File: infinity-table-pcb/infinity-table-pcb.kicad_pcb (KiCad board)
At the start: 2 copper layers, 40 x 48.9 mm, 10 parts, among them J1 PJ-063AH, J2 Conn_01x05_Male, J3 Conn_01x10_Male

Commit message: pcb first version done, but need to rework a bit
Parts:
- removed C2: 100nF, Capacitor_SMD:C_0805_2012Metric
- removed IO2, IO3, IO5, IO6: SolderJumper_3_Open, Jumper:SolderJumper-3_P1.3mm_Open_Pad1.0x1.5mm
- added C3: 0,1uF, Capacitor_SMD:C_0805_2012Metric, F.Cu at (156.5, 116.1)
- added C4: 1nF, Capacitor_SMD:C_0805_2012Metric, B.Cu at (125.8, 108.0)
- added C5: 1nF, Capacitor_SMD:C_0805_2012Metric, B.Cu at (126.2, 91.7)
- added R1: R, Resistor_SMD:R_0805_2012Metric, F.Cu at (157.5, 104.3)
- added RV1: R_Potentiometer, Connector_PinHeader_2.54mm:PinHeader_1x03_P2.54mm_Vertical, B.Cu at (113.8, 76.7)
- added SW1: SW_Push_Dual, kicad-ss-libs:Push Button 12x12mm, F.Cu at (116.6, 108.0)
- added SW2: SW_Push_Dual, kicad-ss-libs:Push Button 12x12mm, F.Cu at (116.6, 89.9)
- added U1: TXS0108EPW, Package_SO:TSSOP-20_4.4x6.5mm_P0.65mm, F.Cu at (154.6, 110.2)
- A1, J3: moved to B.Cu
- C1: value 100nF -> 0,1uF
- J1: footprint SS_connectors:CUI_PJ-063AH-1 -> kicad-ss-libs:CUI_PJ-063AH; moved to B.Cu
- J2: value Conn_01x05_Male -> Conn_01x04_Male; footprint Connector_PinHeader_2.54mm:PinHeader_1x05_P2.54mm_Vertical -> Connector_PinHeader_2.54mm:PinHeader_1x04_P2.54mm_Vertical; moved to B.Cu
- moved C1 39.0 mm to (153.5, 116.1), turned to 90 degrees
- moved J2 31.4 mm to (162.8, 87.6)
- moved J1 28.6 mm to (155.9, 77.7), turned to 0 degrees
- moved A1 16.9 mm to (146.0, 79.8), turned to 180 degrees
- moved J3 2.96 mm to (162.8, 101.1)
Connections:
- A1 pad 1: D1 -> unconnected-(A1-Pad1)
- A1 pad 10: (no net) -> Net-(A1-Pad10)
- A1 pad 11: (no net) -> Net-(A1-Pad11)
- A1 pad 12: D9 -> Net-(A1-Pad12)
- A1 pad 13: D10 -> Net-(A1-Pad13)
- A1 pad 14: (no net) -> Net-(A1-Pad14)
- A1 pad 15: (no net) -> Net-(A1-Pad15)
- A1 pad 16: (no net) -> Net-(A1-Pad16)
- A1 pad 17: (no net) -> unconnected-(A1-Pad17)
- A1 pad 18: (no net) -> unconnected-(A1-Pad18)
- A1 pad 19: (no net) -> Net-(A1-Pad19)
- A1 pad 2: D0 -> unconnected-(A1-Pad2)
- A1 pad 20: (no net) -> unconnected-(A1-Pad20)
- A1 pad 21: Net-(A1-Pad21) -> unconnected-(A1-Pad21)
- A1 pad 22: Net-(A1-Pad22) -> unconnected-(A1-Pad22)
- A1 pad 23: (no net) -> unconnected-(A1-Pad23)
- A1 pad 24: Net-(A1-Pad24) -> unconnected-(A1-Pad24)
- A1 pad 25: Net-(A1-Pad25) -> unconnected-(A1-Pad25)
- A1 pad 26: (no net) -> unconnected-(A1-Pad26)
- A1 pad 27: Net-(A1-Pad27) -> +5V
- A1 pad 28: (no net) -> unconnected-(A1-Pad28)
- A1 pad 3: (no net) -> unconnected-(A1-Pad3)
- A1 pad 30: Net-(A1-Pad30) -> unconnected-(A1-Pad30)
- A1 pad 5: D2 -> unconnected-(A1-Pad5)
- A1 pad 6: D3 -> Net-(A1-Pad6)
- A1 pad 7: (no net) -> SW2
- A1 pad 8: D5 -> SW1
- A1 pad 9: D6 -> Net-(A1-Pad9)
- C1 pad 1: Net-(A1-Pad30) -> GND
- C1 pad 2: GND -> +5V
- J1 pad 1: Net-(J1-Pad1) -> +5V
- J2 pad 2: (no net) -> +5V
- J2 pad 3: Net-(A1-Pad30) -> Net-(A1-Pad6)
- J2 pad 4: Net-(J1-Pad1) -> unconnected-(J2-Pad4)
- J3 pad 1: Net-(J1-Pad1) -> GND
- J3 pad 10: D0 -> Net-(C3-Pad1)
- J3 pad 2: GND -> Net-(J3-Pad2)
- J3 pad 3: D10 -> Net-(J3-Pad3)
- J3 pad 4: D9 -> Net-(J3-Pad4)
- J3 pad 9: D1 -> Net-(J3-Pad9)
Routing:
- net +5V: track 0.00 -> 105.2 mm, vias 0 -> 1
- net D1: track 39.9 -> 0.00 mm, vias 2 -> 0
- net Net-(A1-Pad30): track 39.6 -> 0.00 mm, vias 2 -> 0
- net Net-(A1-Pad19): track 0.00 -> 39.0 mm
- net Net-(A1-Pad9): track 0.00 -> 38.6 mm
- net D10: track 37.9 -> 0.00 mm
- net Net-(A1-Pad12): track 0.00 -> 37.7 mm
- net D9: track 37.5 -> 0.00 mm
- net Net-(A1-Pad10): track 0.00 -> 37.4 mm
- net Net-(A1-Pad11): track 0.00 -> 37.2 mm
- net SW1: track 0.00 -> 34.2 mm
- net D0: track 34.2 -> 0.00 mm, vias 2 -> 0
- net Net-(A1-Pad21): track 31.5 -> 0.00 mm, vias 1 -> 0
- net Net-(A1-Pad27): track 28.2 -> 0.00 mm, vias 2 -> 0
- net Net-(A1-Pad13): track 0.00 -> 26.2 mm
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- removed copper zone on B.Cu, net Net-(J1-Pad1)
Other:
- board size 40 x 48.9 mm -> 61 x 55.9 mm
- net class Default removed
- board text removed: "5V"
- board text removed: "A2"
- board text removed: "A3"
- board text removed: "A5"
- board text removed: "A6"
- board text removed: "D0/Rx"
- board text removed: "D1/Tx"
- board text removed: "D10"
- board text removed: "D2"
- board text removed: "D3"
- board text removed: "D5"
- board text removed: "D6"
- board text removed: "D9"
- board text removed: "GND"
- board text removed: "IO2"
- board text removed: "IO3"
- board text removed: "IO5"
- board text removed: "IO6"
- board text removed: "Sami Sorell"
- board text removed: "Tiny Arduino Breakout Board"
- board text removed: "Vin"
- board text removed: "Vout"

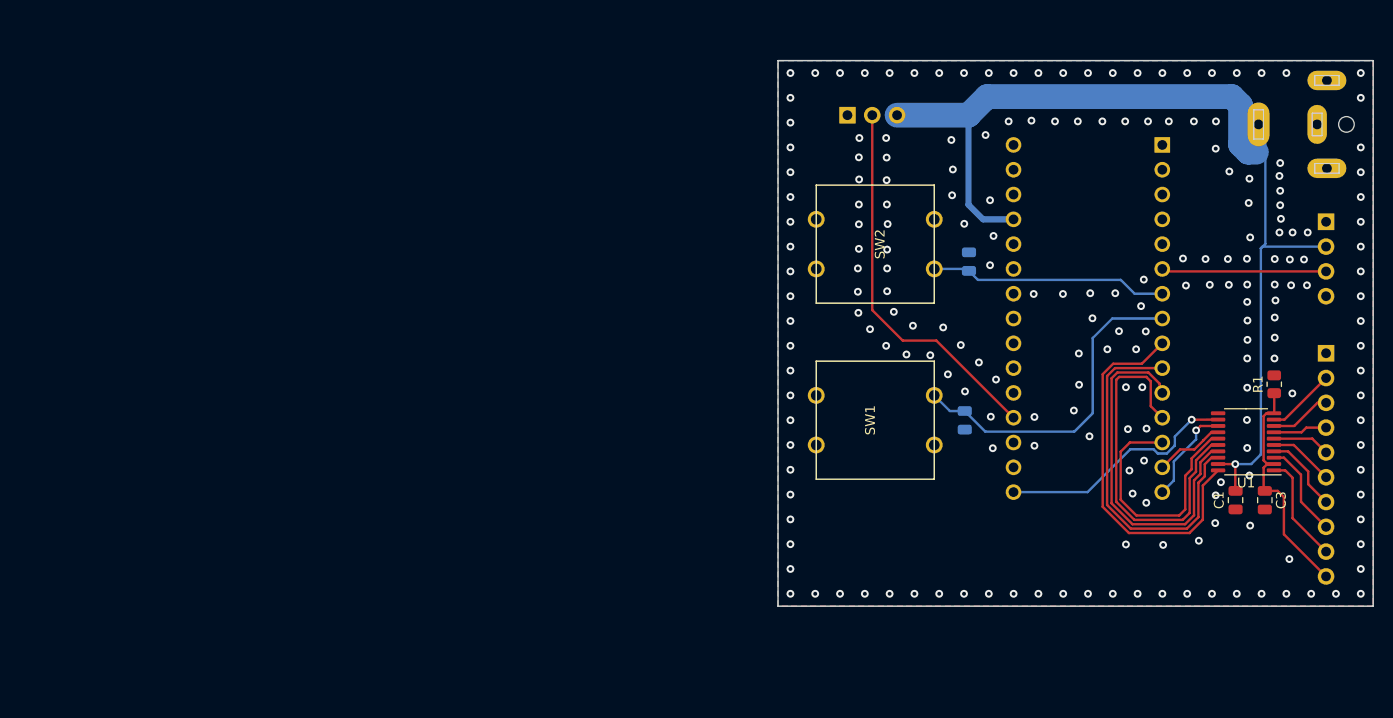
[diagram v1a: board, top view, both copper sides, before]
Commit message: pcb ver 2 done. Maybe potentiometer footprint needs to be checked
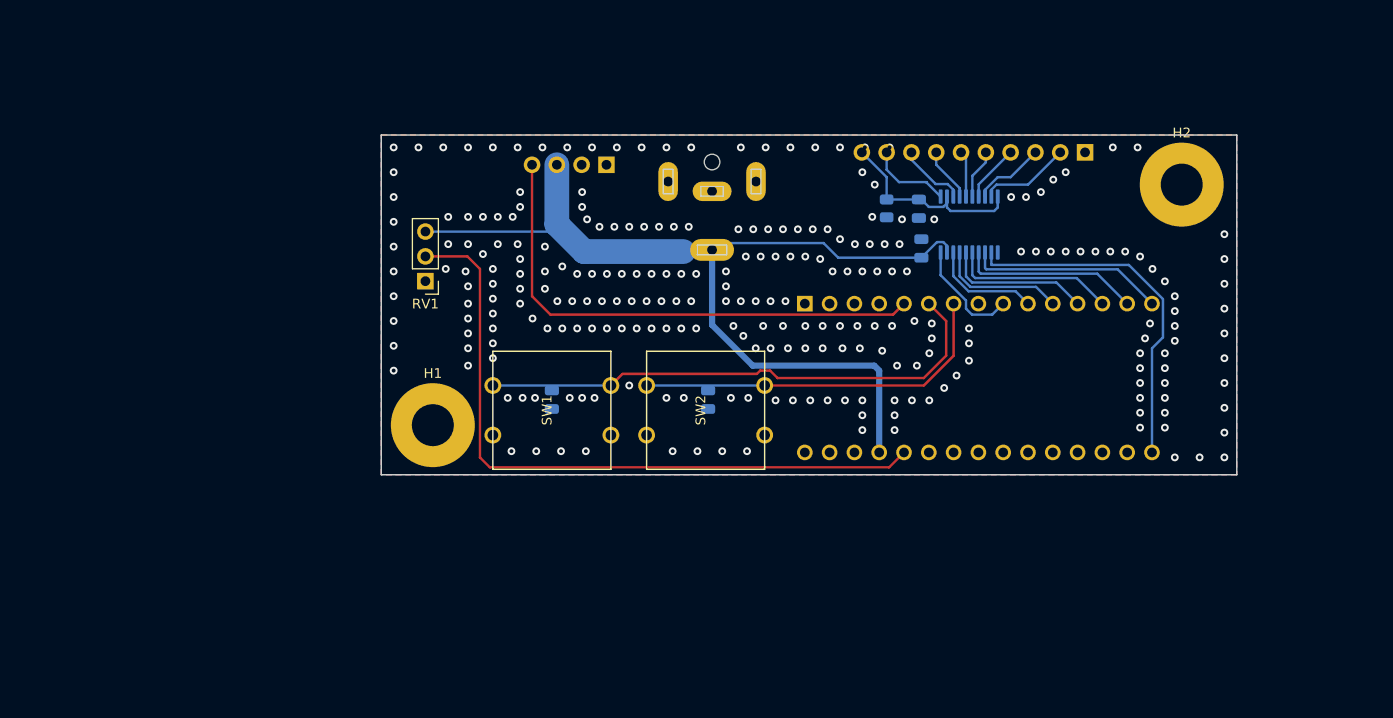
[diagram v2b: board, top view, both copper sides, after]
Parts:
- added H1: MountingHole_Pad, MountingHole:MountingHole_4.3mm_M4_Pad, F.Cu at (71.3, 108.5)
- added H2: MountingHole_Pad, MountingHole:MountingHole_4.3mm_M4_Pad, F.Cu at (148.0, 83.8)
- C1, C3, R1, U1: moved to B.Cu
- RV1: moved to F.Cu
- moved J2 73.9 mm to (89.1, 81.8), turned to 90 degrees
- moved J1 57.4 mm to (99.9, 90.5), turned to 90 degrees
- moved RV1 46.5 mm to (70.6, 93.7), turned to 180 degrees
- moved C3 46.3 mm to (121.1, 86.3)
- moved R1 43.6 mm to (117.8, 86.3), turned to -90 degrees
- moved C4 42.3 mm to (83.5, 105.9)
- moved C1 41.2 mm to (121.4, 90.4), turned to -90 degrees
- moved A1 40.1 mm to (109.4, 96.0), turned to -90 degrees
- moved U1 36.1 mm to (126.3, 87.9), turned to -90 degrees
- moved SW1 33.1 mm to (83.5, 106.9)
- moved J3 32.1 mm to (138.1, 80.5), turned to 90 degrees
- moved C5 30.2 mm to (99.5, 105.9), turned to -90 degrees
- moved SW2 24.3 mm to (99.3, 106.9), turned to -90 degrees
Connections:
- A1 pad 19: Net-(A1-Pad19) -> unconnected-(A1-Pad19)
- A1 pad 26: unconnected-(A1-Pad26) -> Net-(RV1-Pad2)
- A1 pad 5: unconnected-(A1-Pad5) -> Net-(A1-Pad5)
- A1 pad 6: Net-(A1-Pad6) -> SW1
- A1 pad 8: SW1 -> unconnected-(A1-Pad8)
- J2 pad 2: +5V -> GND
- J2 pad 3: Net-(A1-Pad6) -> +5V
- J2 pad 4: unconnected-(J2-Pad4) -> Net-(A1-Pad5)
- RV1 pad 2: Net-(A1-Pad19) -> Net-(RV1-Pad2)
- SW1 pad 3: unconnected-(SW1-Pad3) -> SW1
- SW2 pad 1: unconnected-(SW2-Pad1) -> SW2
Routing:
- net Net-(RV1-Pad2): track 0.00 -> 69.9 mm
- net Net-(A1-Pad5): track 0.00 -> 52.8 mm
- net Net-(A1-Pad19): track 39.0 -> 0.00 mm
- net Net-(A1-Pad9): track 38.6 -> 11.4 mm
- net Net-(A1-Pad10): track 37.4 -> 10.8 mm
- net Net-(A1-Pad11): track 37.2 -> 12.7 mm
- net Net-(A1-Pad12): track 37.7 -> 14.6 mm
- net SW1: track 34.2 -> 54.4 mm
- net Net-(A1-Pad6): track 16.9 -> 0.00 mm
- net SW2: track 24.4 -> 38.0 mm
- net Net-(A1-Pad16): track 24.9 -> 36.5 mm, vias 1 -> 0
- net Net-(A1-Pad14): track 7.21 -> 18.1 mm
- net +5V: track 105.2 -> 95.4 mm, vias 1 -> 0
- net Net-(A1-Pad13): track 26.2 -> 16.4 mm
- net Net-(A1-Pad15): track 10.2 -> 19.8 mm, vias 1 -> 0
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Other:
- board size 61 x 55.9 mm -> 87.6 x 34.8 mm

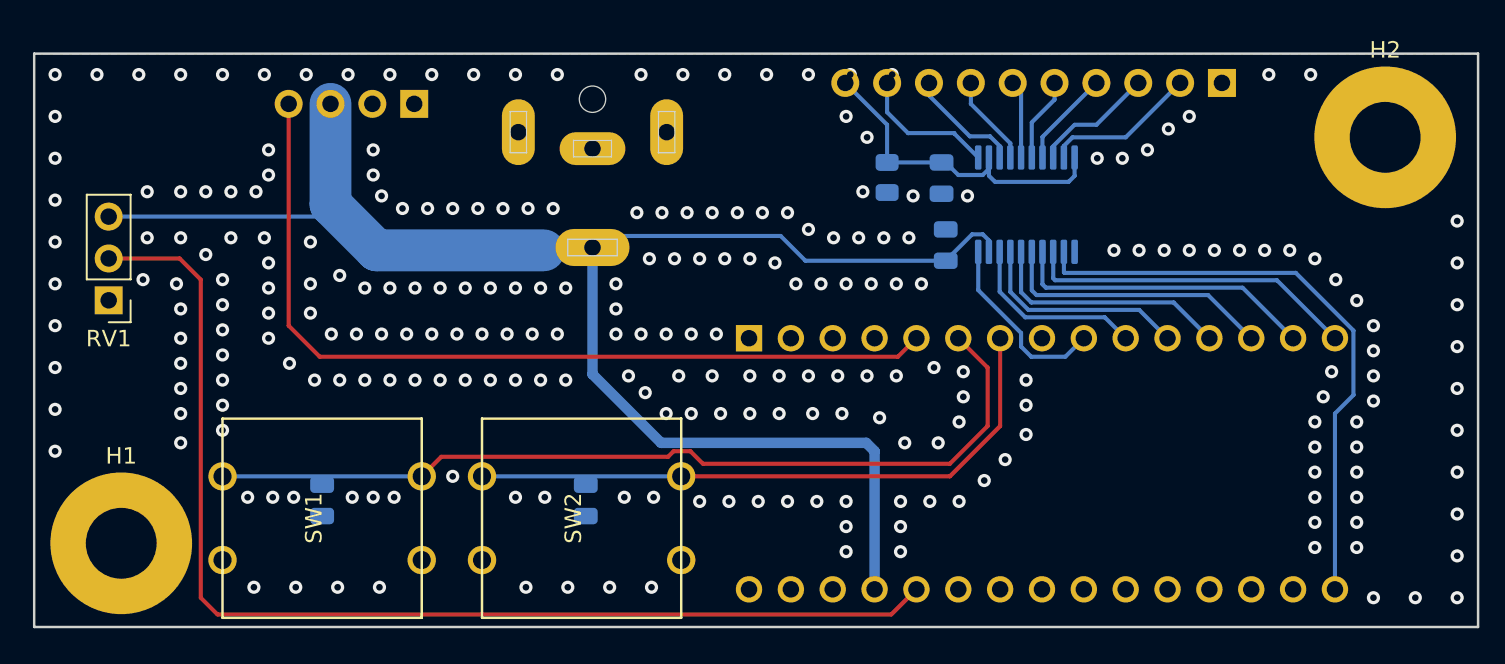
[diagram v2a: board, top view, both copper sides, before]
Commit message: Flip pcb design
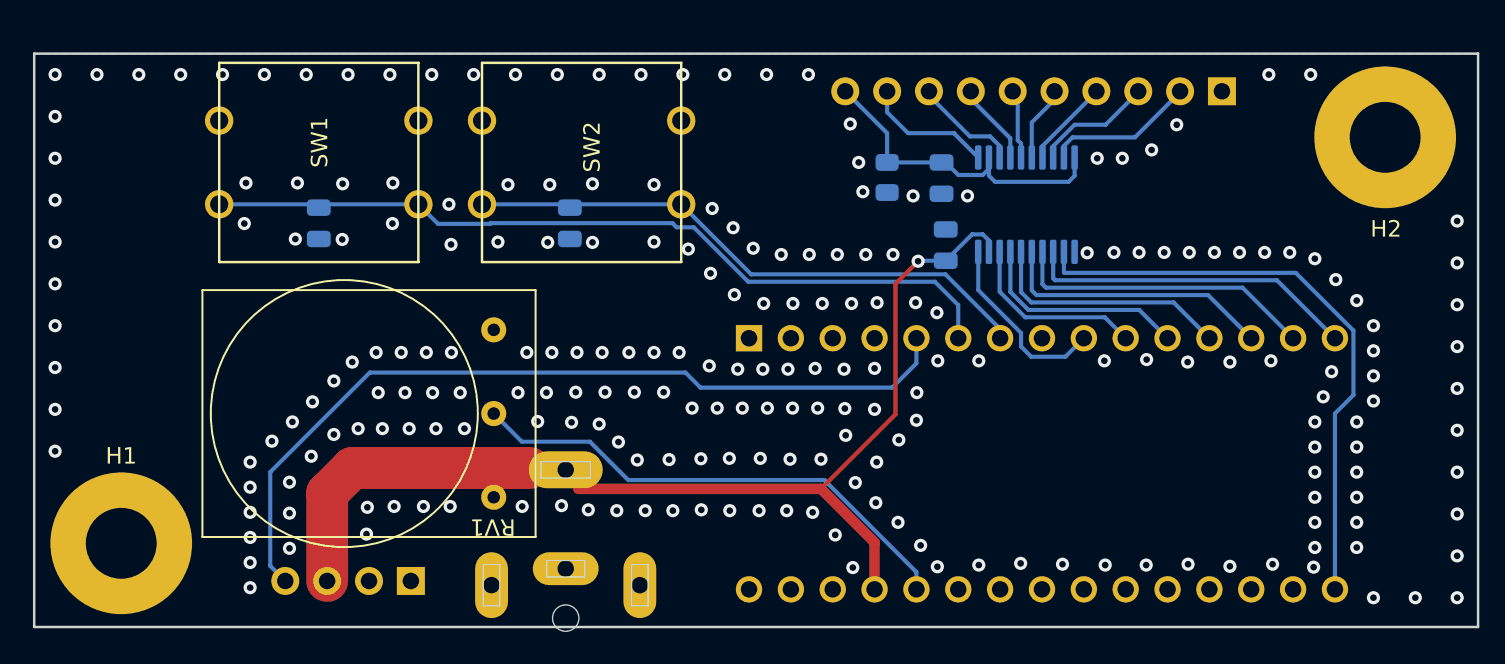
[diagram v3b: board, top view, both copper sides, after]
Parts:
- RV1: footprint Connector_PinHeader_2.54mm:PinHeader_1x03_P2.54mm_Vertical -> kicad-ss-libs:Potentiometer Thruhole
- moved J2 29.0 mm to (88.9, 110.7)
- moved RV1 26.2 mm to (93.9, 105.7)
- moved SW1 21.6 mm to (83.3, 85.3), turned to 90 degrees
- moved SW2 21.6 mm to (99.3, 85.3), turned to 90 degrees
- moved C5 16.8 mm to (98.6, 89.0)
- moved C4 16.8 mm to (83.3, 89.0)
- moved J1 13.6 mm to (98.3, 104.0), turned to -90 degrees
- moved J3 0.51 mm to (138.1, 81.0)
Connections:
- RV1 pad 1: GND -> +5V
- RV1 pad 3: +5V -> GND
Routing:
- net Net-(A1-Pad26): track 69.9 -> 30.7 mm
- net +5V: track 95.4 -> 62.5 mm, vias 0 -> 1
- net SW1: track 54.4 -> 49.5 mm
- net SW2: track 38.0 -> 35.2 mm
- net Net-(J3-Pad7): track 6.21 -> 4.55 mm
- net Net-(A1-Pad5): track 52.8 -> 51.2 mm
- net Net-(J3-Pad8): track 7.71 -> 6.26 mm
- net Net-(J3-Pad5): track 5.52 -> 4.50 mm
- net Net-(J3-Pad2): track 10.0 -> 9.11 mm
- net Net-(J3-Pad4): track 5.88 -> 5.32 mm
- net Net-(C3-Pad1): track 19.9 -> 19.3 mm
- net GND: vias 250 -> 229

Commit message: add silk
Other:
- board text added: "infinity-table v2 Sami Sorell"
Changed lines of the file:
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@@
   (gr_line (start 66.04 113.538) (end 66.04 78.74) (layer "Edge.Cuts") (width 0.15))
   (gr_line (start 153.67 113.538) (end 66.04 113.538) (layer "Edge.Cuts") (width 0.15))
+  (gr_text "infinity-table v2\nSami Sorell" (at 71.755 90.7542 90) (layer "F.SilkS")
+    (effects (font (size 1.5 1.5) (thickness 0.3)))
+  )
   (via (at 110.2614 97.8916) (size 0.8) (drill 0.4) (layers "F.Cu" "B.Cu") (free) (net 1))
   (via (at 115.6462 93.9038) (size 0.8) (drill 0.4) (layers "F.Cu" "B.Cu") (free) (net 1))

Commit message: power supply on the right, led connector on the left. idk
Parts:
- C4: moved to F.Cu
- RV1: footprint kicad-ss-libs:Potentiometer Thruhole -> kicad-ss-libs:Potentiometer Pads
- moved C4 40.0 mm to (119.9, 105.2), turned to -90 degrees
- moved SW1 33.0 mm to (110.8, 103.6)
- moved C5 21.6 mm to (120.1, 90.1), turned to 90 degrees
- moved SW2 11.7 mm to (110.8, 87.6)
- moved RV1 10.7 mm to (88.9, 96.3)
- moved J2 10.2 mm to (78.7, 109.7), turned to -90 degrees
- moved C1 2.59 mm to (124.0, 90.4)
- moved J3 2.59 mm to (140.7, 81.0)
- moved R1 2.59 mm to (120.4, 86.3)
- moved C3 2.59 mm to (123.7, 86.3)
- moved U1 2.59 mm to (128.8, 87.9)
- moved J1 1.20 mm to (97.1, 104.0)
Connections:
- J2 pad 3: +5V -> Net-(A1-Pad5)
- J2 pad 4: Net-(A1-Pad5) -> +5V
- SW1 pad 1: SW1 -> unconnected-(SW1-Pad1)
- SW2 pad 1: SW2 -> unconnected-(SW2-Pad1)
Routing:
- net SW1: track 49.5 -> 14.9 mm
- net SW2: track 35.2 -> 10.5 mm
- net +5V: track 62.5 -> 82.4 mm
- net Net-(A1-Pad26): track 30.7 -> 39.6 mm, vias 0 -> 1
- net Net-(A1-Pad5): track 51.2 -> 44.2 mm
- net Net-(A1-Pad9): track 11.4 -> 6.82 mm
- net Net-(A1-Pad16): track 36.5 -> 33.7 mm
- net Net-(A1-Pad15): track 19.8 -> 17.1 mm
- net Net-(A1-Pad14): track 18.1 -> 15.7 mm
- net Net-(A1-Pad10): track 10.8 -> 8.45 mm
- net Net-(A1-Pad12): track 14.6 -> 12.3 mm
- net Net-(A1-Pad11): track 12.7 -> 10.4 mm
- net Net-(A1-Pad13): track 16.4 -> 14.1 mm
- net GND: vias 229 -> 244
- net (no net): vias 0 -> 8

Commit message: pcb done again
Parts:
- C5: moved to F.Cu
- moved J2 21.3 mm to (100.1, 109.5), turned to 90 degrees
- moved J1 14.3 mm to (82.8, 104.0)
- moved R1 0.87 mm to (120.5, 85.4)
- moved C3 0.76 mm to (123.7, 85.5)
- moved C5 0.33 mm to (120.5, 90.1)
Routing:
- net Net-(A1-Pad26): track 39.6 -> 50.5 mm, vias 1 -> 0
- net +5V: track 82.4 -> 92.3 mm, vias 1 -> 0
- net Net-(A1-Pad5): track 44.2 -> 34.7 mm
- net SW1: track 14.9 -> 16.0 mm
- net SW2: track 10.5 -> 11.3 mm
- net GND: vias 244 -> 180
- net (no net): vias 8 -> 0
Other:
- outline, holes or cut-outs redrawn
- board text added: "Sami Sorell"
- board text added: "infinity-table v2"
- board text removed: "infinity-table v2 Sami Sorell"
